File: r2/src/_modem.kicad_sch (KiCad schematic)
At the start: 38 parts, among them J1 , J11 SMA, J12 U_FL-R-SMT-1_10_, J13 JAE_SIM_Card_SF72S006, J2 , J3 , J4 , J5 , J6 , J7 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

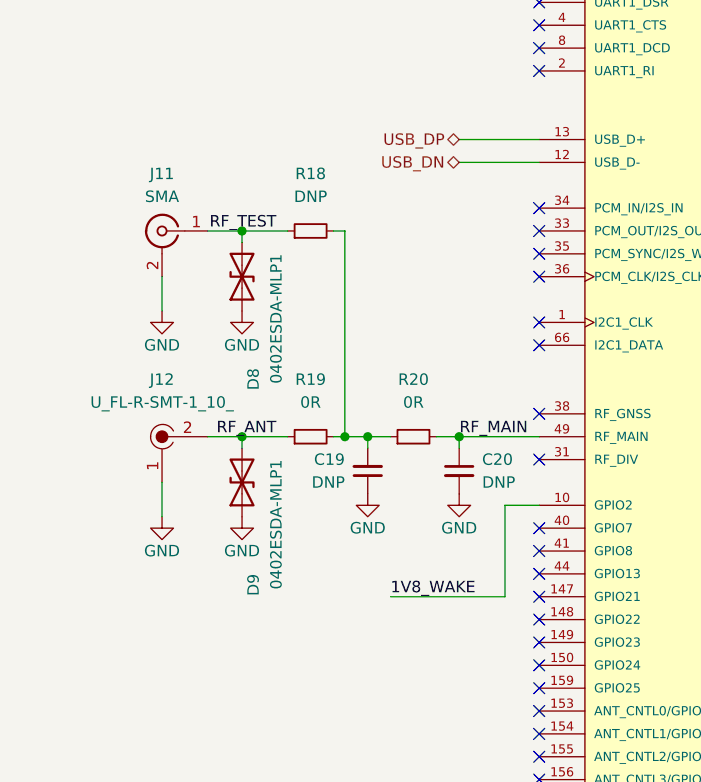
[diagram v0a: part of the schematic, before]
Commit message: Route RF area
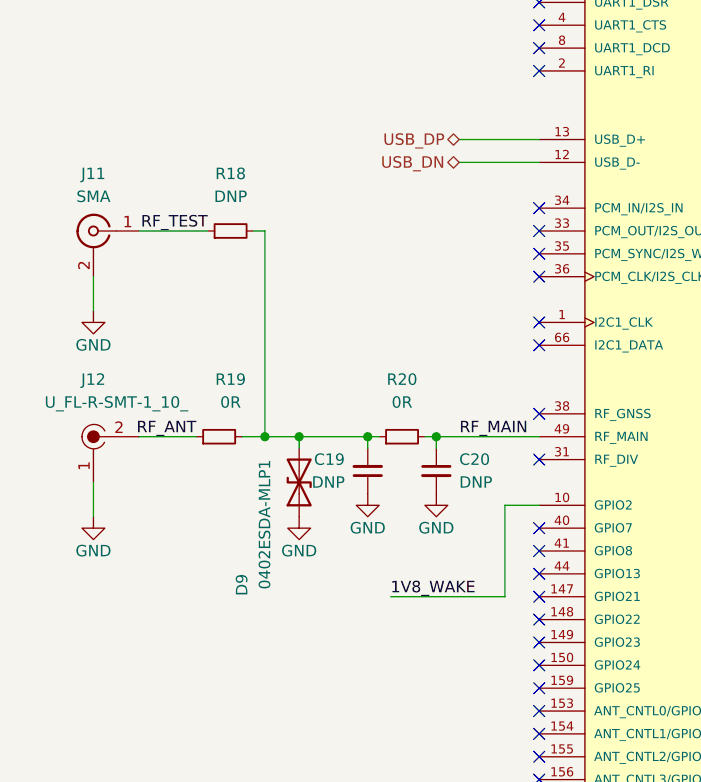
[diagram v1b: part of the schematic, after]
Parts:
- removed D8: 0402ESDA-MLP1, Diode_SMD:D_0402_1005Metric, symbol Device:D_TVS
- J11: footprint Connector_Coaxial:SMA_Amphenol_901-144_Vertical -> Connector_Coaxial:SMA_Amphenol_132134-10_Vertical
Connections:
- net RF_ANT: no longer D9.2 (A2)
- net at C19.2, R18.2, R19.2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: now also D9.2 (A2)
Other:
- moved on the sheet: C20, D9, J11, J12, R18, R19, R20

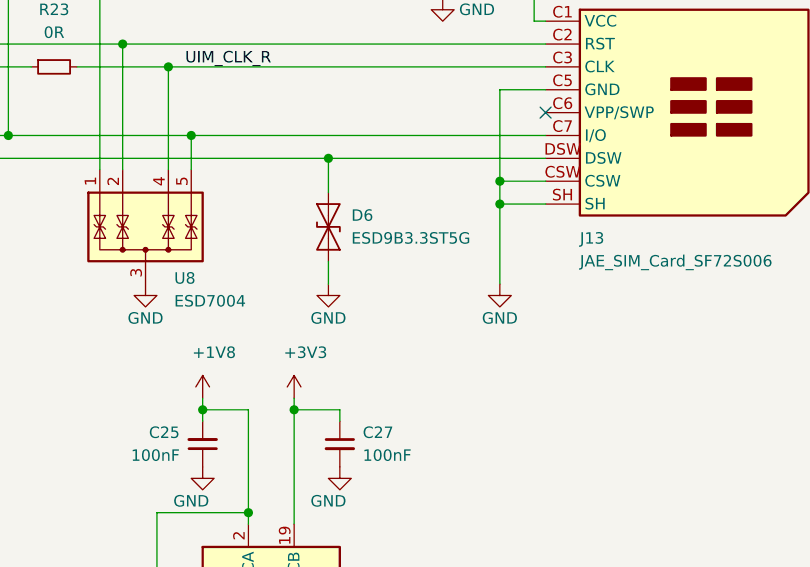
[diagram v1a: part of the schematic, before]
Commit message: Set TVS diode to the same type as used in the RF section
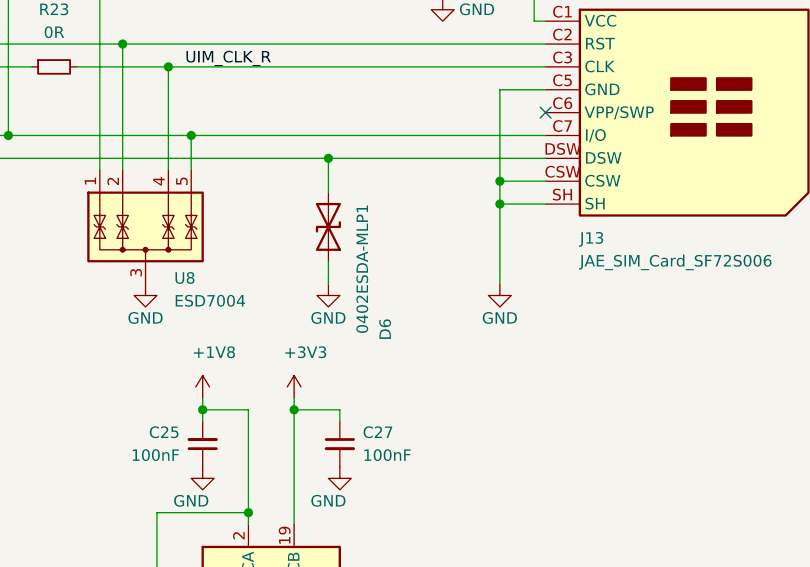
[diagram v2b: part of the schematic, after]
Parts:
- removed D6: ESD9B3.3ST5G, Diode_SMD:D_SOD-923, symbol Diode:ESD9B3.3ST5G
- added D6: 0402ESDA-MLP1, Diode_SMD:D_0402_1005Metric, symbol Device:D_TVS
- U7: footprint jeffmakes-footprints:Cellular_Modem-Sierra-Wireless-module-CF3-ringCD -> MODULE_WP7504
- U8: footprint jeffmakes-footprints:USON-10_2.5x1.0mm_P0.5mm -> Package_SON:USON-10_2.5x1.0mm_P0.5mm
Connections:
- net GND: now also D6.1 (A1)
- net UIM_SIM_DET: now also D6.2 (A2)

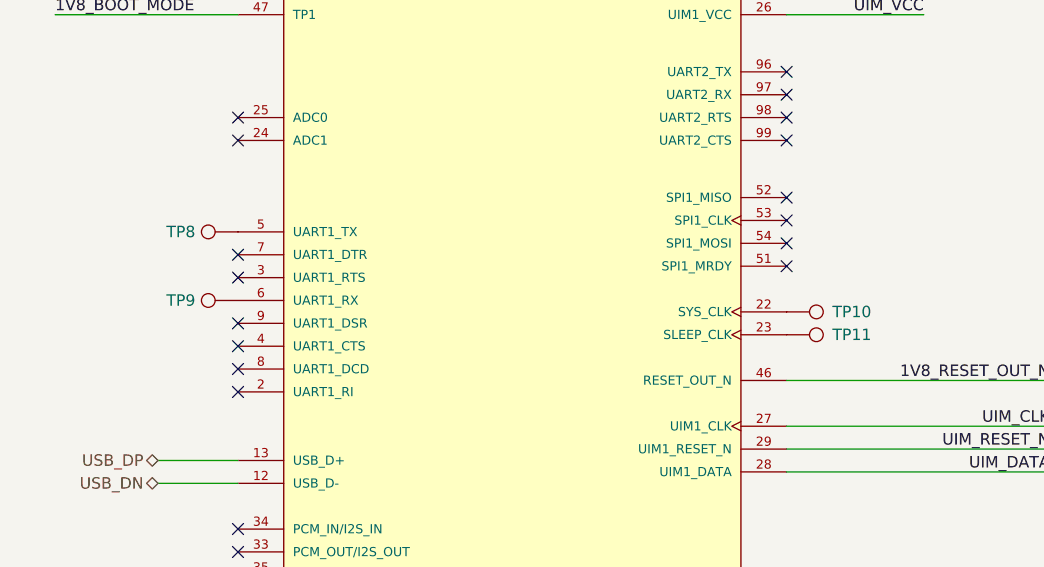
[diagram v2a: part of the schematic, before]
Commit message: Change testpoint names from TPx to Tx
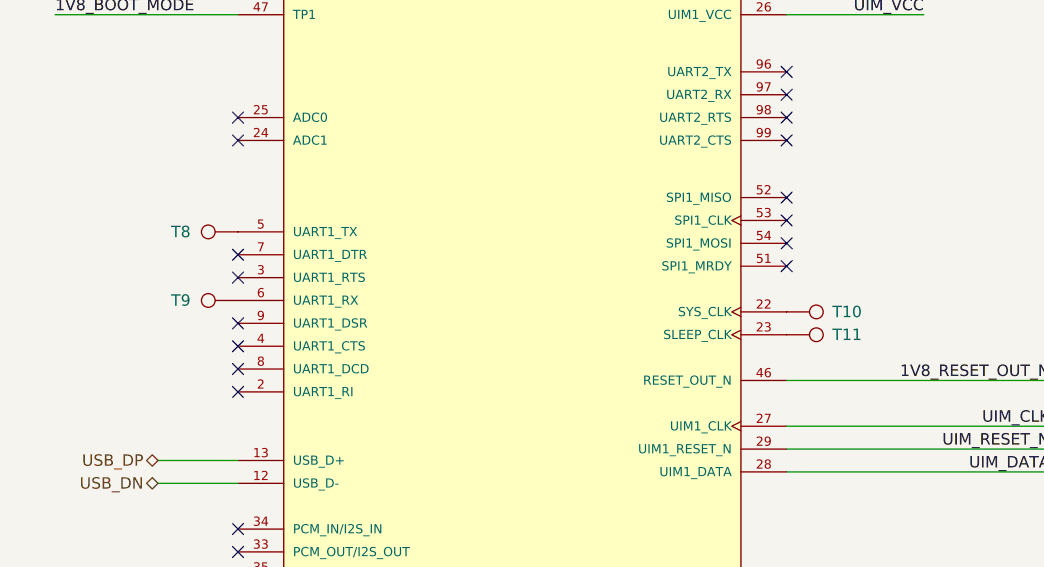
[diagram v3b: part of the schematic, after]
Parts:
- renumbered TP10 to T10, TP11 to T11, TP8 to T8, TP9 to T9

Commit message: Fix some missing footprint references. Change USB micro symbol for correct pin naming
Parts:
- U7: footprint MODULE_WP7504 -> jeffmakes-footprints:Cellular_Modem-Sierra-Wireless-module-CF3-ringCD

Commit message: Loads of weird library bollocks resolved.
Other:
- moved on the sheet: T8, T9

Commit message: Replace TVS arrays with feed-through numbering
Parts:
- U8: footprint Package_SON:USON-10_2.5x1.0mm_P0.5mm -> jeffmakes-footprints:USON-10_2.5x1.0mm_P0.5mm
